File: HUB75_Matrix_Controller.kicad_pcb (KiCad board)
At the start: 4 copper layers, 59 x 53 mm, 61 parts, among them J1 USB_C_Receptacle_USB2.0_16P, J2 Barrel_Jack_MountingPin, J3 Screw_Terminal_01x02, J4 Micro_SD_Card_Det2, J5 SFH11-PBPC-D08-ST-BK, SW1 EN, SW2 BOOT, U1 LSM6DSOTR, U2 AMS1117-3.3, U3 USBLC6-2SC6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

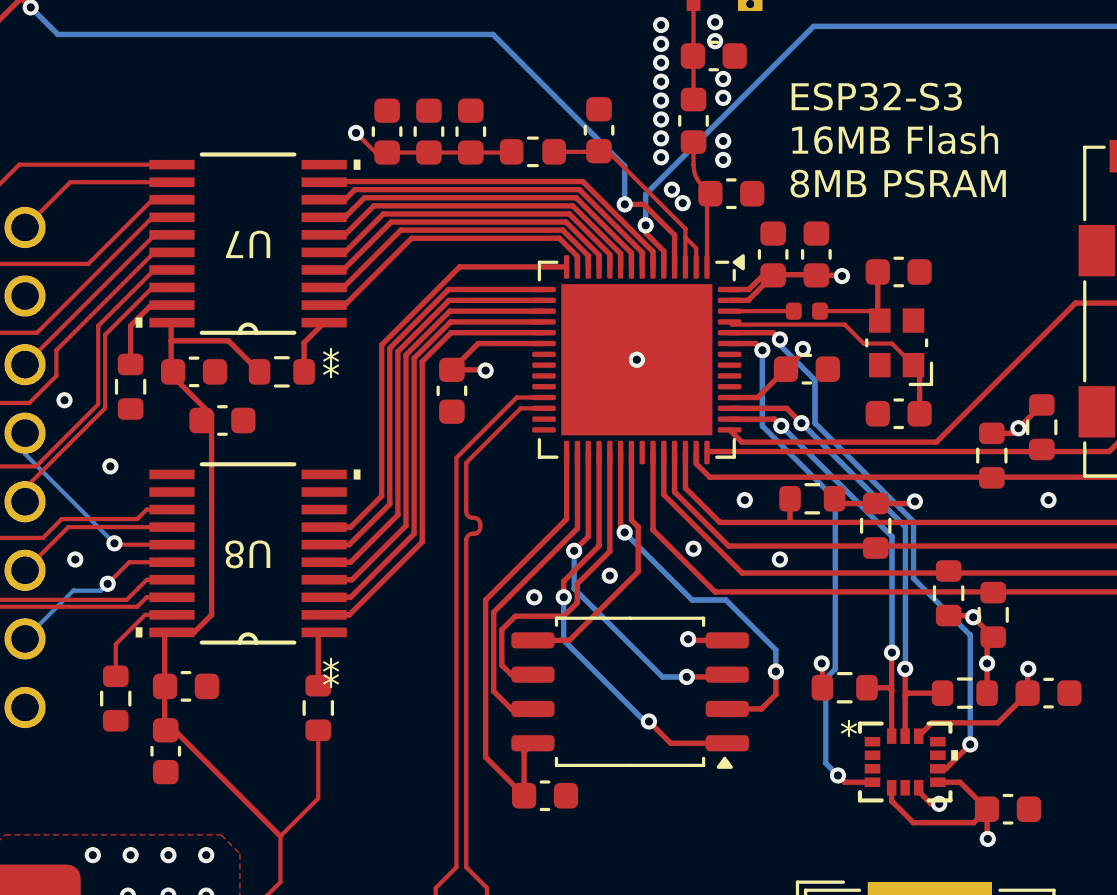
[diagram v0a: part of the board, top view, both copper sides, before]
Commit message: ESP -> HUB75
Option to ignore Level Shifter
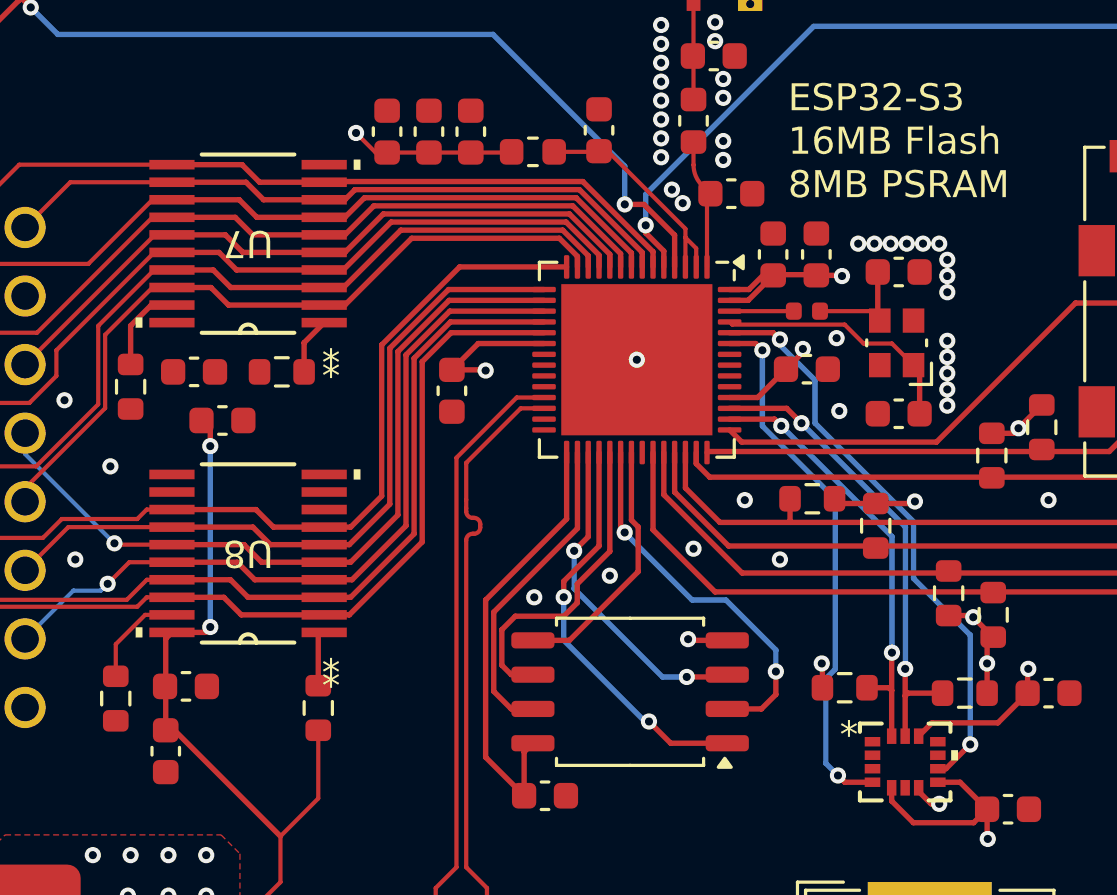
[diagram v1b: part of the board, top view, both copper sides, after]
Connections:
- U6 pad 10: G2_ESP -> G2
- U6 pad 11: B2_ESP -> B2
- U6 pad 12: A_ESP -> A
- U6 pad 13: B_ESP -> B
- U6 pad 14: C_ESP -> C
- U6 pad 15: D_ESP -> D
- U6 pad 16: E_ESP -> E
- U6 pad 17: LAT_ESP -> LAT
- U6 pad 18: OE_ESP -> OE
- U6 pad 19: CLK_ESP -> CLK
- U6 pad 6: R1_ESP -> R1
- U6 pad 7: G1_ESP -> G1
- U6 pad 8: B1_ESP -> B1
- U6 pad 9: R2_ESP -> R2
- U7 pad 2: B_ESP -> B
- U7 pad 3: A_ESP -> A
- U7 pad 4: B2_ESP -> B2
- U7 pad 5: G2_ESP -> G2
- U7 pad 6: R2_ESP -> R2
- U7 pad 7: B1_ESP -> B1
- U7 pad 8: G1_ESP -> G1
- U7 pad 9: R1_ESP -> R1
- U8 pad 2: CLK_ESP -> CLK
- U8 pad 3: OE_ESP -> OE
- U8 pad 4: LAT_ESP -> LAT
- U8 pad 5: E_ESP -> E
- U8 pad 6: D_ESP -> D
- U8 pad 7: C_ESP -> C
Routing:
- net CLK: track 8.62 -> 31.2 mm
- net C: track 8.91 -> 31.3 mm
- net OE: track 13.4 -> 35.7 mm
- net LAT: track 6.62 -> 28.8 mm
- net E: track 7.60 -> 29.5 mm
- net D: track 6.10 -> 27.7 mm
- net R1: track 8.94 -> 28.7 mm
- net G1: track 6.13 -> 25.5 mm
- net B1: track 9.46 -> 28.4 mm
- net R2: track 10.2 -> 28.8 mm
- net G2: track 7.43 -> 25.6 mm
- net B2: track 11.3 -> 29.1 mm
- net A: track 13.2 -> 30.6 mm
- net B: track 10.6 -> 27.6 mm
- net CLK_ESP: track 16.7 -> 0.00 mm
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
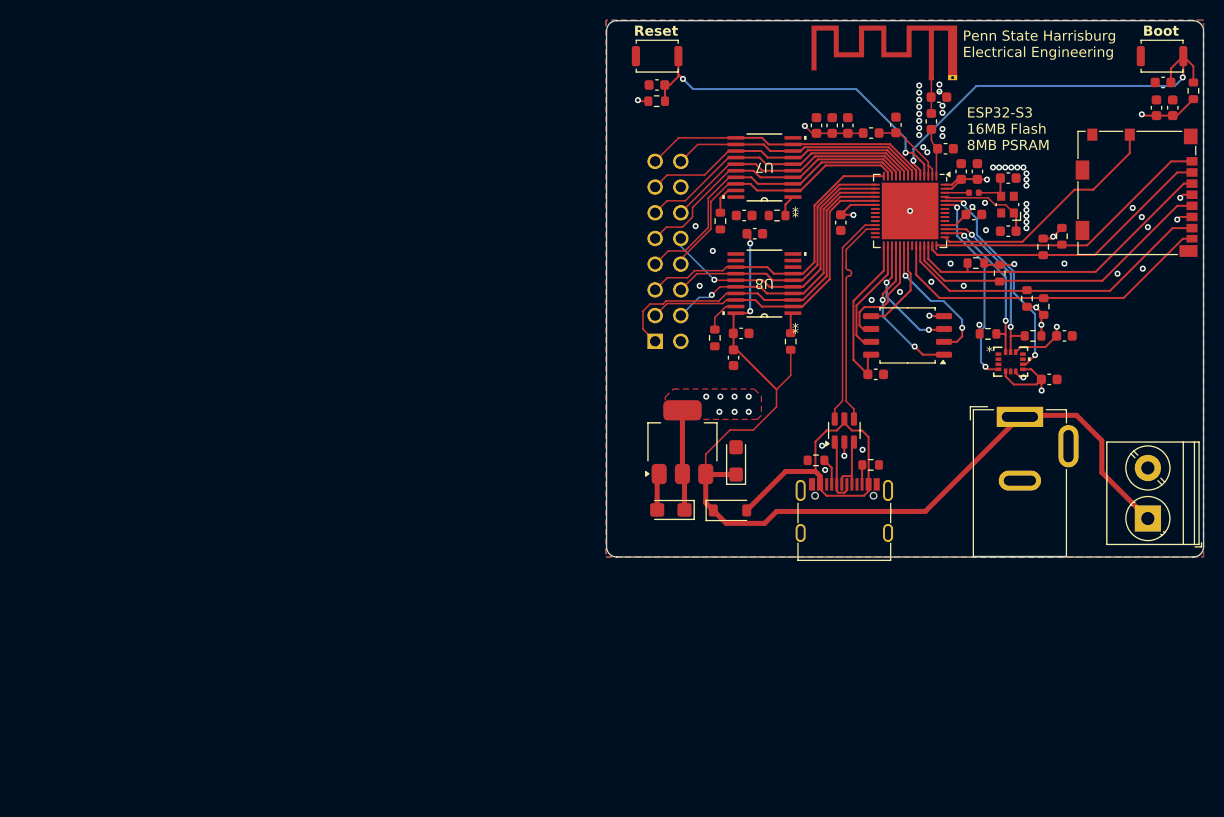
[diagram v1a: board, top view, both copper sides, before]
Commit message: Silkscreen Updates
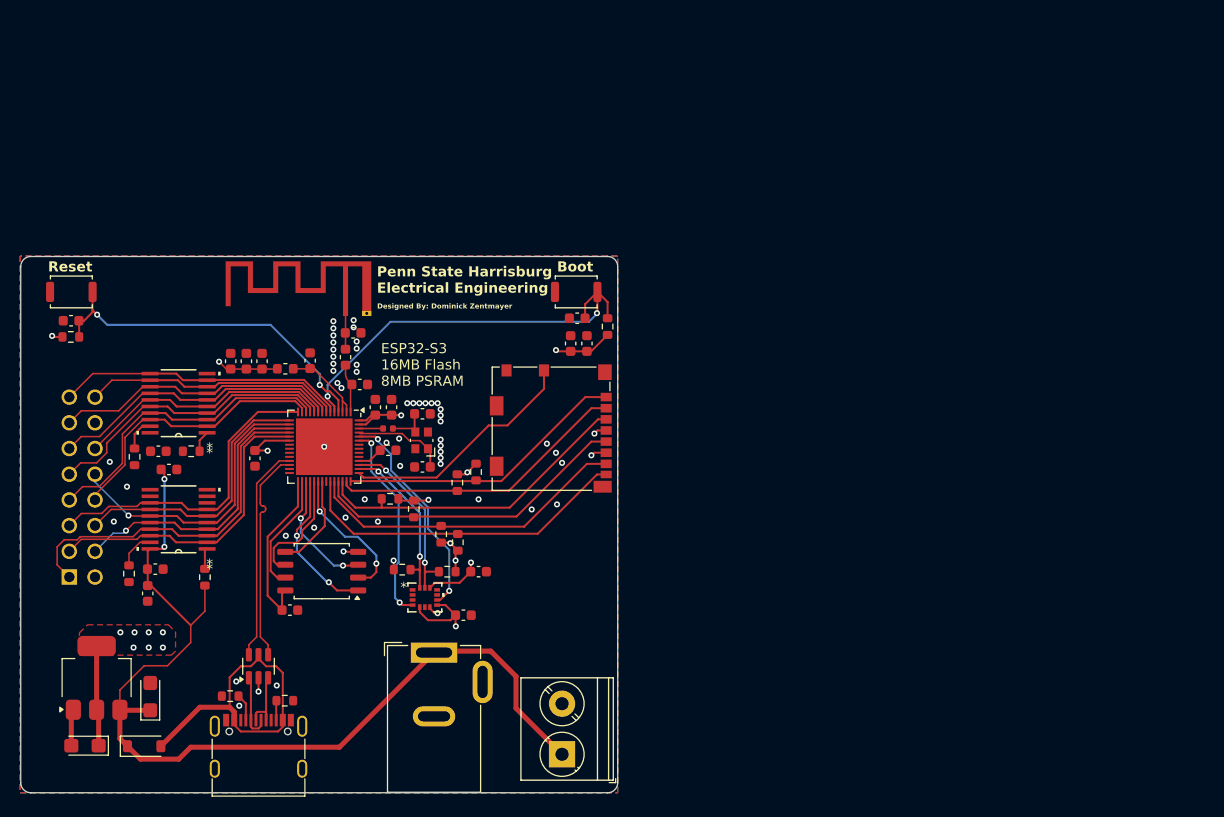
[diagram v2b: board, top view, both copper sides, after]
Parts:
- moved L3 62.4 mm to (145.8, 87.9)
- moved R9 62.4 mm to (162.8, 99.2)
- moved U4 62.4 mm to (149.3, 107.9)
- moved C1 62.4 mm to (163.3, 112.2)
- moved C10 62.4 mm to (140.3, 87.2)
- moved C11 62.4 mm to (141.9, 87.2)
- moved C12 62.4 mm to (143.4, 87.2)
- moved C13 62.4 mm to (142.8, 96.8)
- moved C14 62.4 mm to (148.2, 87.1)
- moved C15 62.4 mm to (155.9, 96.0)
- moved C16 62.4 mm to (154.7, 91.7)
- moved C17 62.4 mm to (156.2, 91.7)
- moved C2 62.4 mm to (132.4, 120.3)
- moved C21 62.4 mm to (174.6, 82.9)
- moved C22 62.4 mm to (134.2, 97.8)
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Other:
- board text added: "B - 08 C - 09 D - 10 E - 11 LAT - 12 OE - 13 CLK - 14"
- board text added: "Designed By: Dominick Zentmayer"
- board text added: "HUB75 Pinout: R1 - 01 G1 - 02 B1 - 03 R2 - 04 G2 - 05 B2 - 06 A - 07"

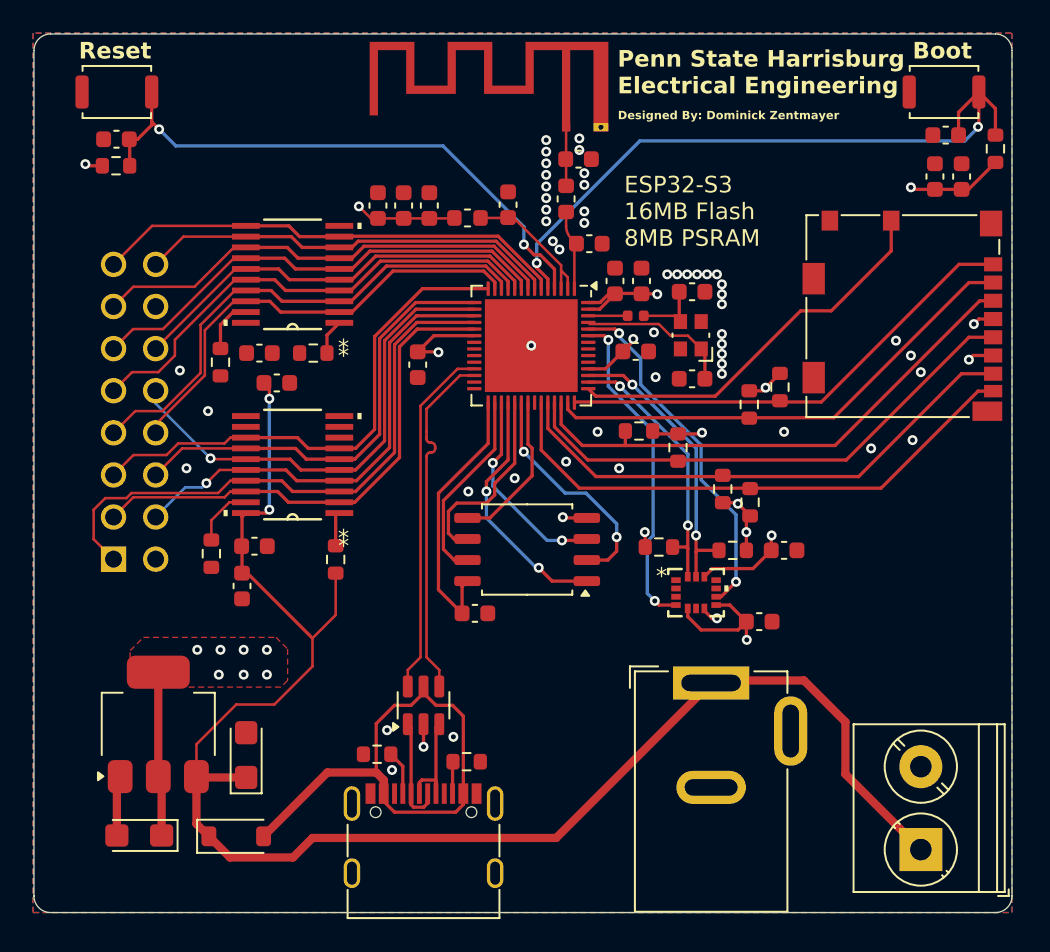
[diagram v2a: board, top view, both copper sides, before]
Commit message: v2, fixed SD and USB
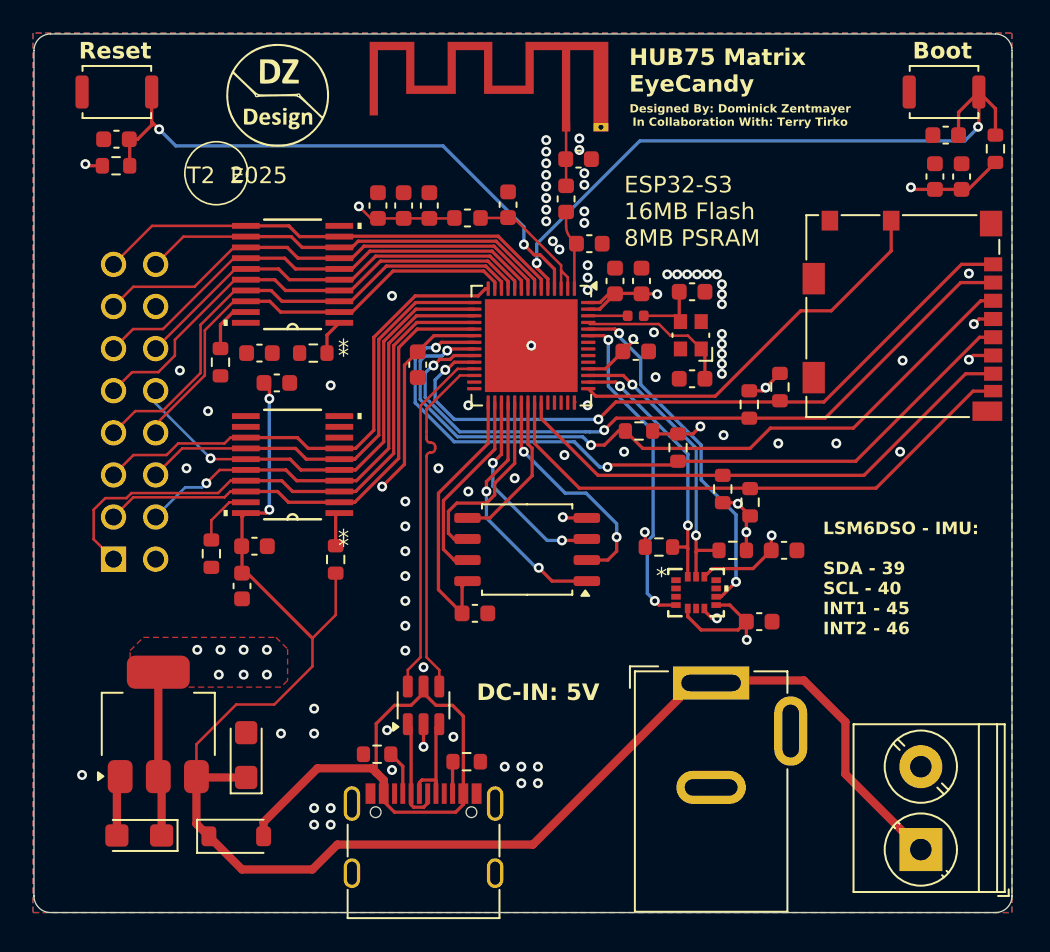
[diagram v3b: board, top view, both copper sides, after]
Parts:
- added G***: LOGO, LOGO, F.Cu at (134.3, 80.5)
- J5: footprint Project Footprints:SULLINS_SFH11-PBPC-D08-ST-BK -> footprints:SULLINS_SFH11-PBPC-D08-ST-BK
- U1: footprint Project Footprints:LGA-14L_2P5X3X0P86_STM -> footprints:LGA-14L_2P5X3X0P86_STM
- U7, U8: footprint Project Footprints:PW20 -> footprints:PW20
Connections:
- U6 pad 21: unconnected-(U6-GPIO15/ADC2_CH4/XTAL_32K_P-Pad21) -> SD_CLK
- U6 pad 22: unconnected-(U6-GPIO16/ADC2_CH5/XTAL_32K_N-Pad22) -> CMD
- U6 pad 23: unconnected-(U6-GPIO17/ADC2_CH6-Pad23) -> D3
- U6 pad 24: unconnected-(U6-GPIO18/ADC2_CH7-Pad24) -> D2
- U6 pad 36: unconnected-(U6-SPICLK_N/GPIO48-Pad36) -> D1
- U6 pad 37: D1 -> D0
- U6 pad 38: D0 -> unconnected-(U6-GPIO33-Pad38)
- U6 pad 39: SD_CLK -> unconnected-(U6-GPIO34-Pad39)
- U6 pad 40: CMD -> unconnected-(U6-GPIO35-Pad40)
- U6 pad 41: D3 -> unconnected-(U6-GPIO36-Pad41)
- U6 pad 42: D2 -> unconnected-(U6-GPIO37-Pad42)
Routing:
- net SD_CLK: track 31.8 -> 46.3 mm, vias 0 -> 2
- net D3: track 29.7 -> 43.7 mm, vias 0 -> 2
- net CMD: track 32.4 -> 46.2 mm, vias 0 -> 2
- net D2: track 28.7 -> 42.1 mm, vias 0 -> 2
- net +3V3: track 63.1 -> 70.9 mm
- net VBUS: track 30.9 -> 31.6 mm
- net +5V: track 97.0 -> 97.6 mm
- net GND: vias 54 -> 82
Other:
- board text added: "4bit SDMMC: D0 - 47 D1 - 48 D2 - 18 D3 - 17 CLK - 15 CMD - 16 DET - 38"
- board text added: "DC-IN: 5V"
- board text added: "Designed By: Dominick Zentmayer In Collaboration With: Terry Tirko"
- board text added: "E"
- board text added: "HUB75 Matrix EyeCandy"
- board text added: "LSM6DSO - IMU: SDA - 39 SCL - 40 INT1 - 45 INT2 - 46"
- board text added: "T2 2025"
- board text removed: "Designed By: Dominick Zentmayer"
- board text removed: "Penn State Harrisburg Electrical Engineering"

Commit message: v1.1, final changes
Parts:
- removed C22, C23: 1uF, Capacitor_SMD:C_0603_1608Metric
- removed C24, C25: 100nF, Capacitor_SMD:C_0603_1608Metric
- removed R11, R12, R15, R16: 10k, Resistor_SMD:R_0603_1608Metric
- removed U7, U8: SN74HCT245PWR, footprints:PW20
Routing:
- net +5V: track 97.6 -> 61.6 mm, vias 2 -> 0
- net OE: track 35.7 -> 27.7 mm
- net +3V3: track 70.9 -> 65.1 mm
- net LAT: track 28.8 -> 24.3 mm, vias 1 -> 0
- net E: track 29.5 -> 25.2 mm
- net D: track 27.7 -> 23.5 mm
- net C: track 31.3 -> 27.3 mm
- net CLK: track 31.2 -> 27.4 mm, vias 0 -> 1
- net Net-(U8-*OE): track 3.72 -> 0.00 mm
- net Net-(U7-*OE): track 3.28 -> 0.00 mm
- net B: track 27.6 -> 25.2 mm
- net A: track 30.6 -> 28.4 mm
- net Net-(U7-DIR): track 2.13 -> 0.00 mm
- net Net-(U8-DIR): track 2.00 -> 0.00 mm
- net B2: track 29.1 -> 28.0 mm
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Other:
- board text added: "+"
- board text added: "-"
- board text added: "- +"

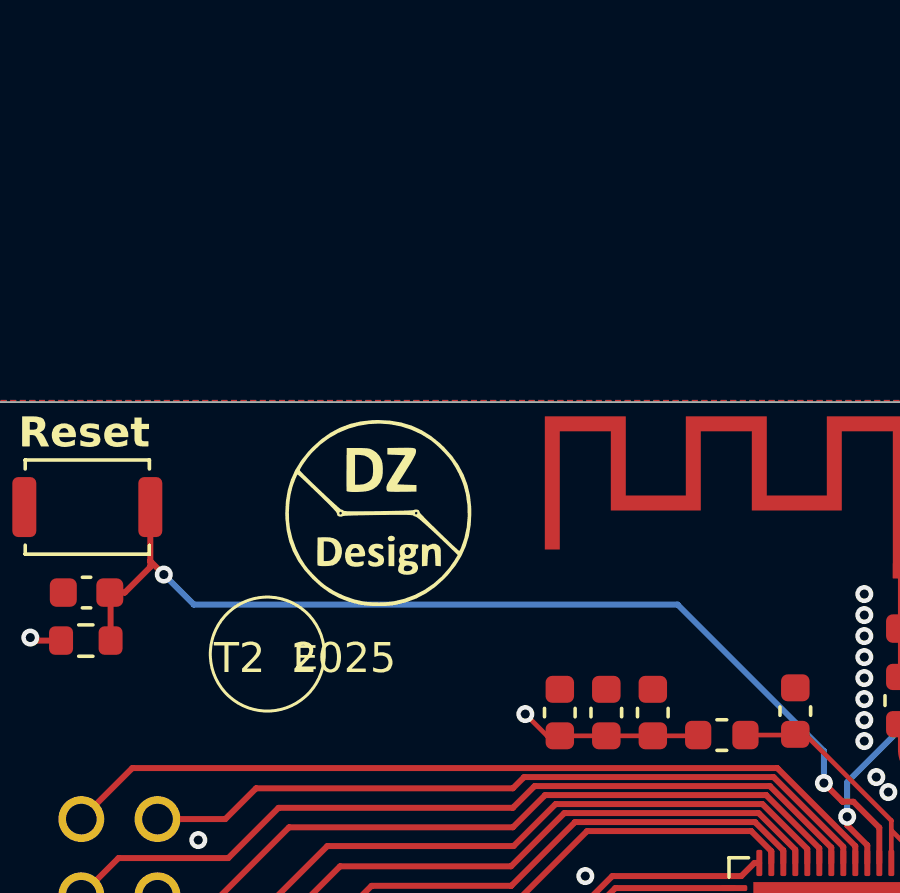
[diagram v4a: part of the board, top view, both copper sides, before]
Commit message: Added code examples
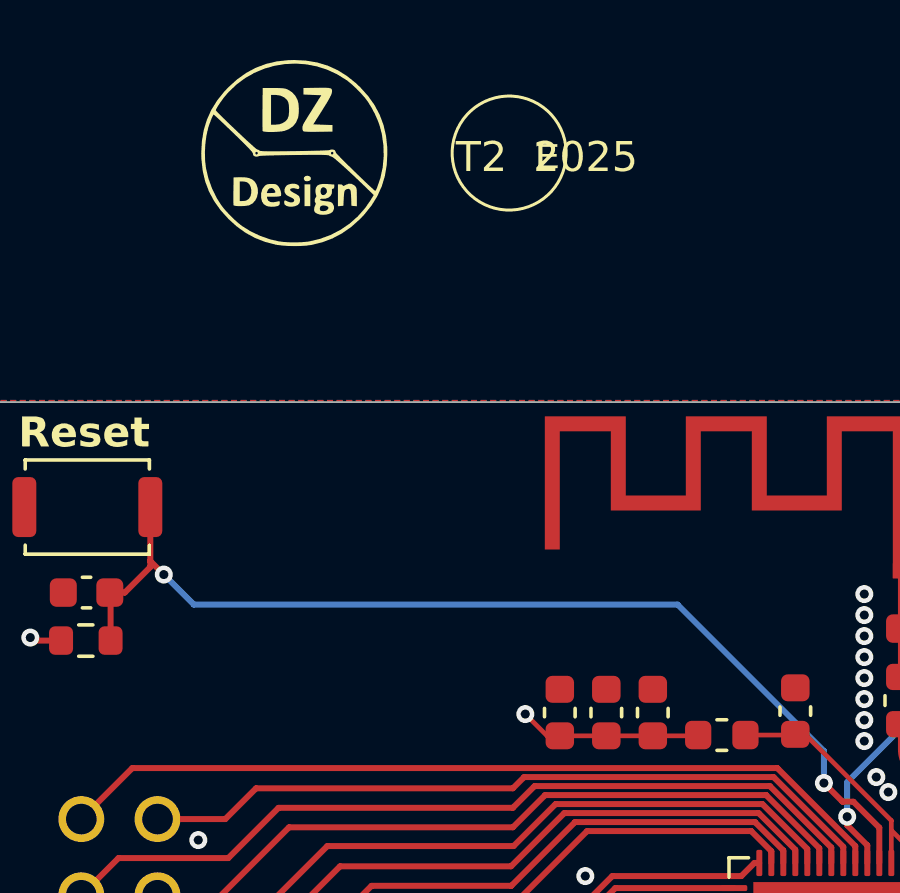
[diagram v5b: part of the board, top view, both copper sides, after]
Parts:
- moved G*** 12.3 mm to (131.5, 68.5)
